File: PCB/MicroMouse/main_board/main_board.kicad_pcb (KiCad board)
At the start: 2 copper layers, 75 x 108.5 mm, 54 parts, among them J1 Conn_01x06, J10 Conn_01x05, J11 Conn_01x02, J12 Conn_01x04, J2 Conn_01x02, J3 Conn_01x04, J4 Conn_01x06, J5 Conn_01x06, J7 Conn_01x06, J8 Conn_01x06, J9 Conn_01x02, U2 LT8608, U3 TB6612FNG, U4 ESP32-WROOM-32U

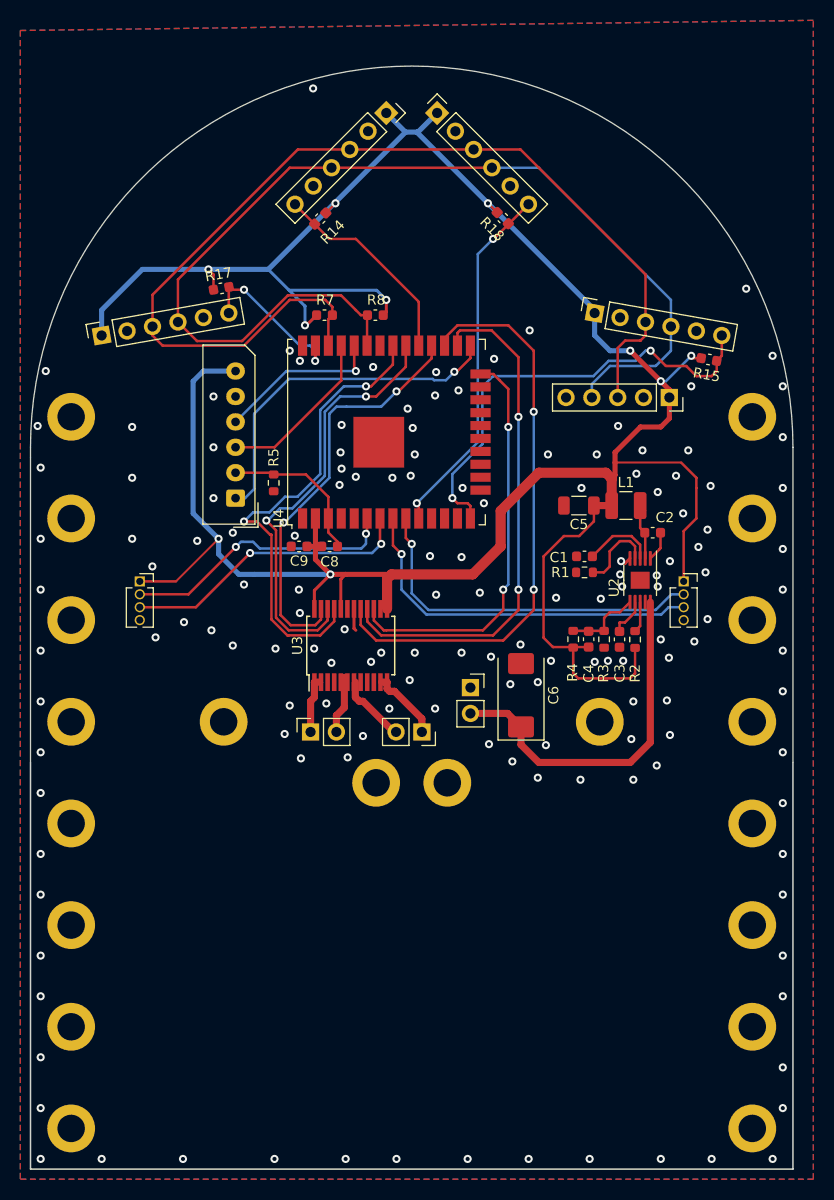
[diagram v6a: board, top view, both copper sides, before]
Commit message: remove atmel from code
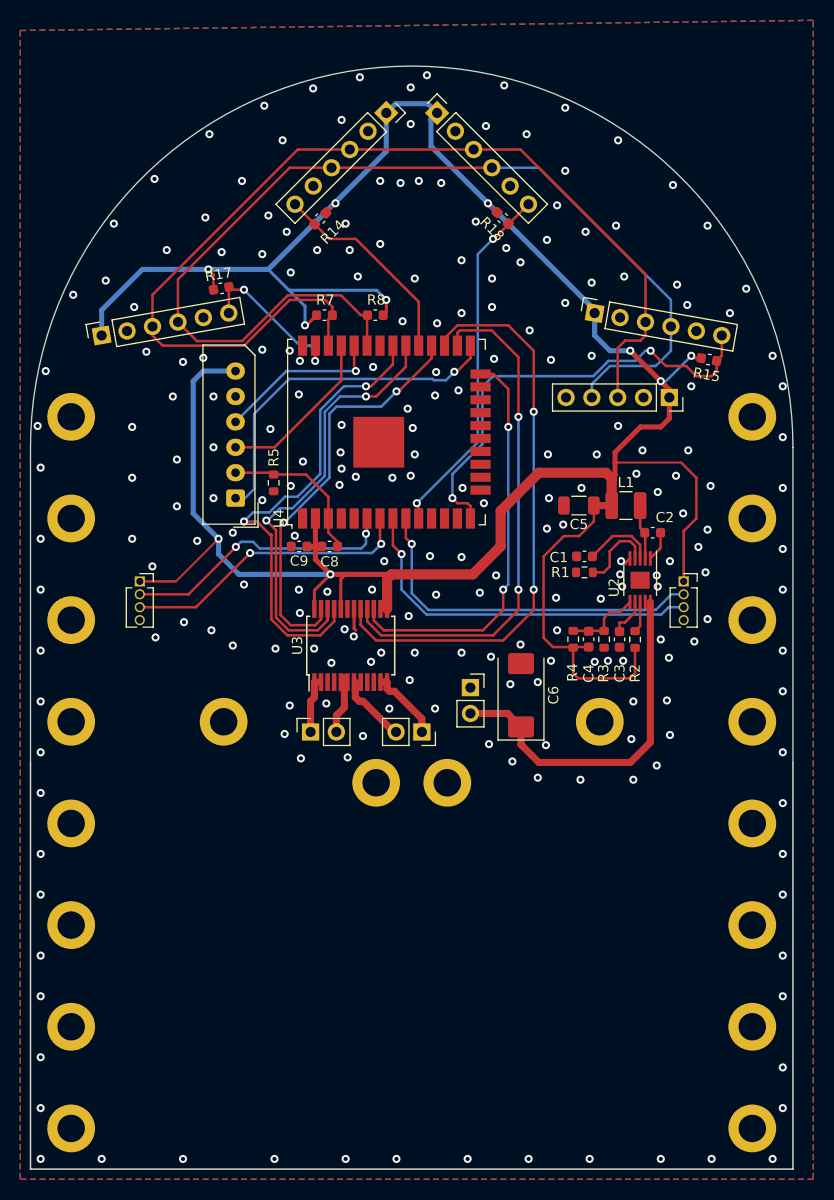
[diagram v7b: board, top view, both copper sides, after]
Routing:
- net 3v3: track 278.4 -> 280.3 mm
- net GND: vias 149 -> 231
